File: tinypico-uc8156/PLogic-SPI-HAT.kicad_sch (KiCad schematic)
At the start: 14 parts, among them J1 C262568, Q1 FET P-CH 60V 620Ma, Q2 MOSFET N-CH 30V 1.4A SC-70-3, U1 TinypicoESP32_Symbol

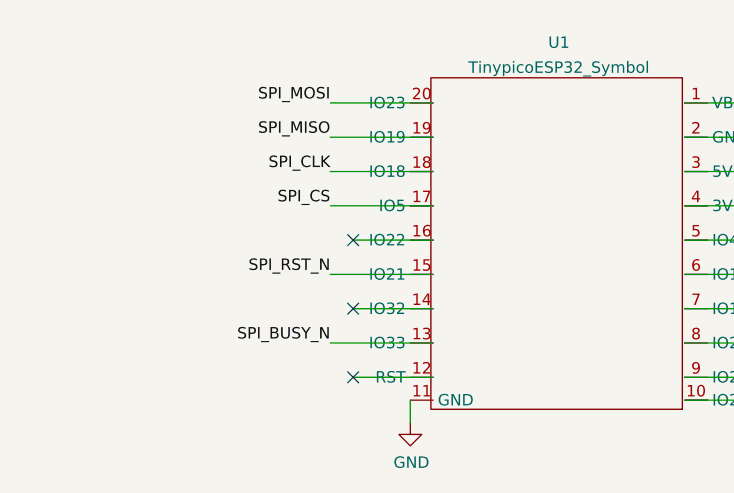
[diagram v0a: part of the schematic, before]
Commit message: Move out RST from IO21->32
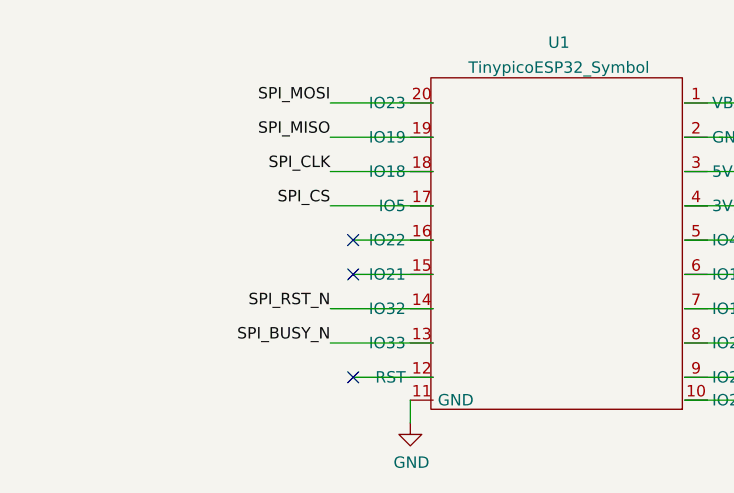
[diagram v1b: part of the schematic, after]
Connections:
- net SPI_RST_N: now also U1.14 (IO32); no longer U1.15 (IO21)
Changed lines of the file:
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@@
   )
   (no_connect (at 146.05 152.4))
+  (no_connect (at 99.06 171.45))
   (no_connect (at 146.05 160.02))
   (no_connect (at 146.05 167.64))
   (no_connect (at 146.05 171.45))
   (no_connect (at 99.06 182.88))
-  (no_connect (at 99.06 175.26))
   (no_connect (at 99.06 167.64))
   (no_connect (at 146.05 185.42))
@@
     (stroke (width 0) (type default) (color 0 0 0 0))
   )
-  (wire (pts (xy 99.06 175.26) (xy 107.95 175.26))
+  (wire (pts (xy 96.52 175.26) (xy 107.95 175.26))
     (stroke (width 0) (type default) (color 0 0 0 0))
   )
@@
     (stroke (width 0) (type default) (color 0 0 0 0))
   )
-  (wire (pts (xy 96.52 171.45) (xy 107.95 171.45))
-    (stroke (width 0) (type default) (color 0 0 0 0))
-  )
   (wire (pts (xy 210.82 123.19) (xy 210.82 125.73))
     (stroke (width 0) (type default) (color 0 0 0 0))
@@
   )
   (wire (pts (xy 101.6 124.46) (xy 99.06 124.46))
+    (stroke (width 0) (type default) (color 0 0 0 0))
+  )
+  (wire (pts (xy 99.06 171.45) (xy 107.95 171.45))
     (stroke (width 0) (type default) (color 0 0 0 0))
   )
@@
     (effects (font (size 1.27 1.27)) (justify right bottom))
   )
-  (label "SPI_RST_N" (at 96.52 171.45 180)
-    (effects (font (size 1.27 1.27)) (justify right bottom))
-  )
   (label "SPI_BUSY_N" (at 218.44 102.87 180)
     (effects (font (size 1.27 1.27)) (justify right bottom))
@@
     (effects (font (size 1.27 1.27)) (justify right bottom))
   )
+  (label "SPI_RST_N" (at 96.52 175.26 180)
+    (effects (font (size 1.27 1.27)) (justify right bottom))
+  )

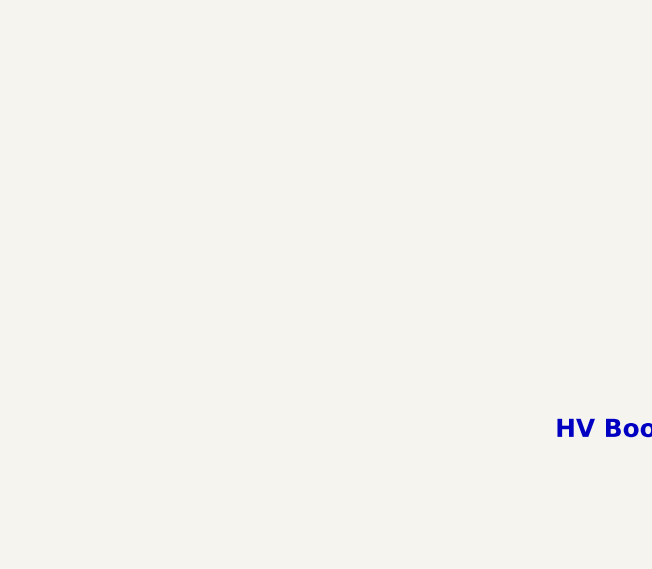
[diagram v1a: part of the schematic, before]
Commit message: Bump uc81156 adapter to REV 1.1, clean up old GBR
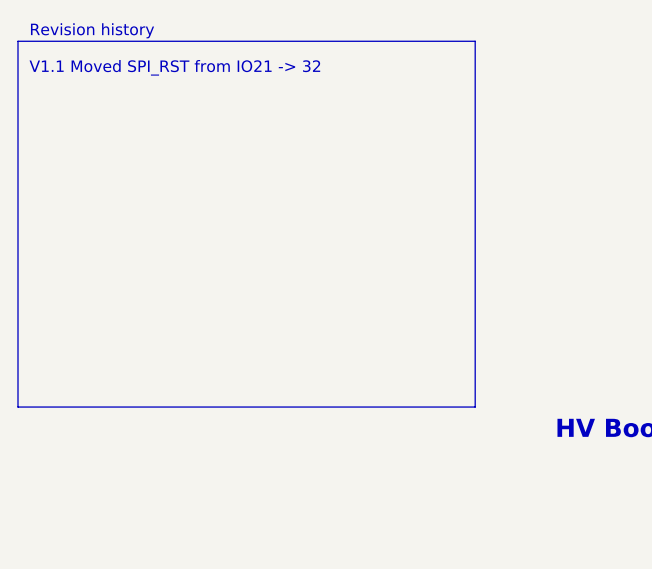
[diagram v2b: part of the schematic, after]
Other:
- note added: "Revision history V1.1 Moved SPI_RST from IO21 -> 32"
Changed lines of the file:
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@@
     (title "PlasticLogic SPI HAT for tinyPico.com ESP32")
     (date "2022-02-12")
-    (rev "1.0")
+    (rev "1.1")
     (company "FASANI CORPORATION")
     (comment 4 "PlasticLogic SPI HAT")
@@
     (stroke (width 0) (type default) (color 0 0 0 0))
   )
+  (polyline (pts (xy 73.66 60.96) (xy 22.86 60.96))
+    (stroke (width 0) (type default) (color 0 0 0 0))
+  )
   (wire (pts (xy 92.71 100.33) (xy 92.71 101.6))
     (stroke (width 0) (type default) (color 0 0 0 0))
@@
     (stroke (width 0) (type default) (color 0 0 0 0))
   )
+  (polyline (pts (xy 22.86 20.32) (xy 22.86 60.96))
+    (stroke (width 0) (type default) (color 0 0 0 0))
+  )
   (wire (pts (xy 76.2 92.71) (xy 92.71 92.71))
     (stroke (width 0) (type default) (color 0 0 0 0))
@@
     (stroke (width 0) (type default) (color 0 0 0 0))
   )
+  (polyline (pts (xy 22.86 20.32) (xy 73.66 20.32))
+    (stroke (width 0) (type default) (color 0 0 0 0))
+  )
   (polyline (pts (xy 214.63 152.4) (xy 214.63 127))
     (stroke (width 0) (type default) (color 0 0 0 0))
@@
     (stroke (width 0) (type default) (color 0 0 0 0))
   )
+  (polyline (pts (xy 73.66 20.32) (xy 73.66 60.96))
+    (stroke (width 0) (type default) (color 0 0 0 0))
+  )
   (wire (pts (xy 151.13 77.47) (xy 119.38 77.47))
     (stroke (width 0) (type default) (color 0 0 0 0))
@@
     (stroke (width 0) (type default) (color 0 0 0 0))
   )
+  (text "Revision history\n\nV1.1 Moved SPI_RST from IO21 -> 32"
+    (at 24.13 24.13 0)
+    (effects (font (size 1.27 1.27)) (justify left bottom))
+  )
   (text "Decoupling" (at 214.63 156.21 180)
